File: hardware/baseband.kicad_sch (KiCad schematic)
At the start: 36 parts, among them U503 MCP4551, U504 MCP4551, U6 MCP6002, U7 MCP6002

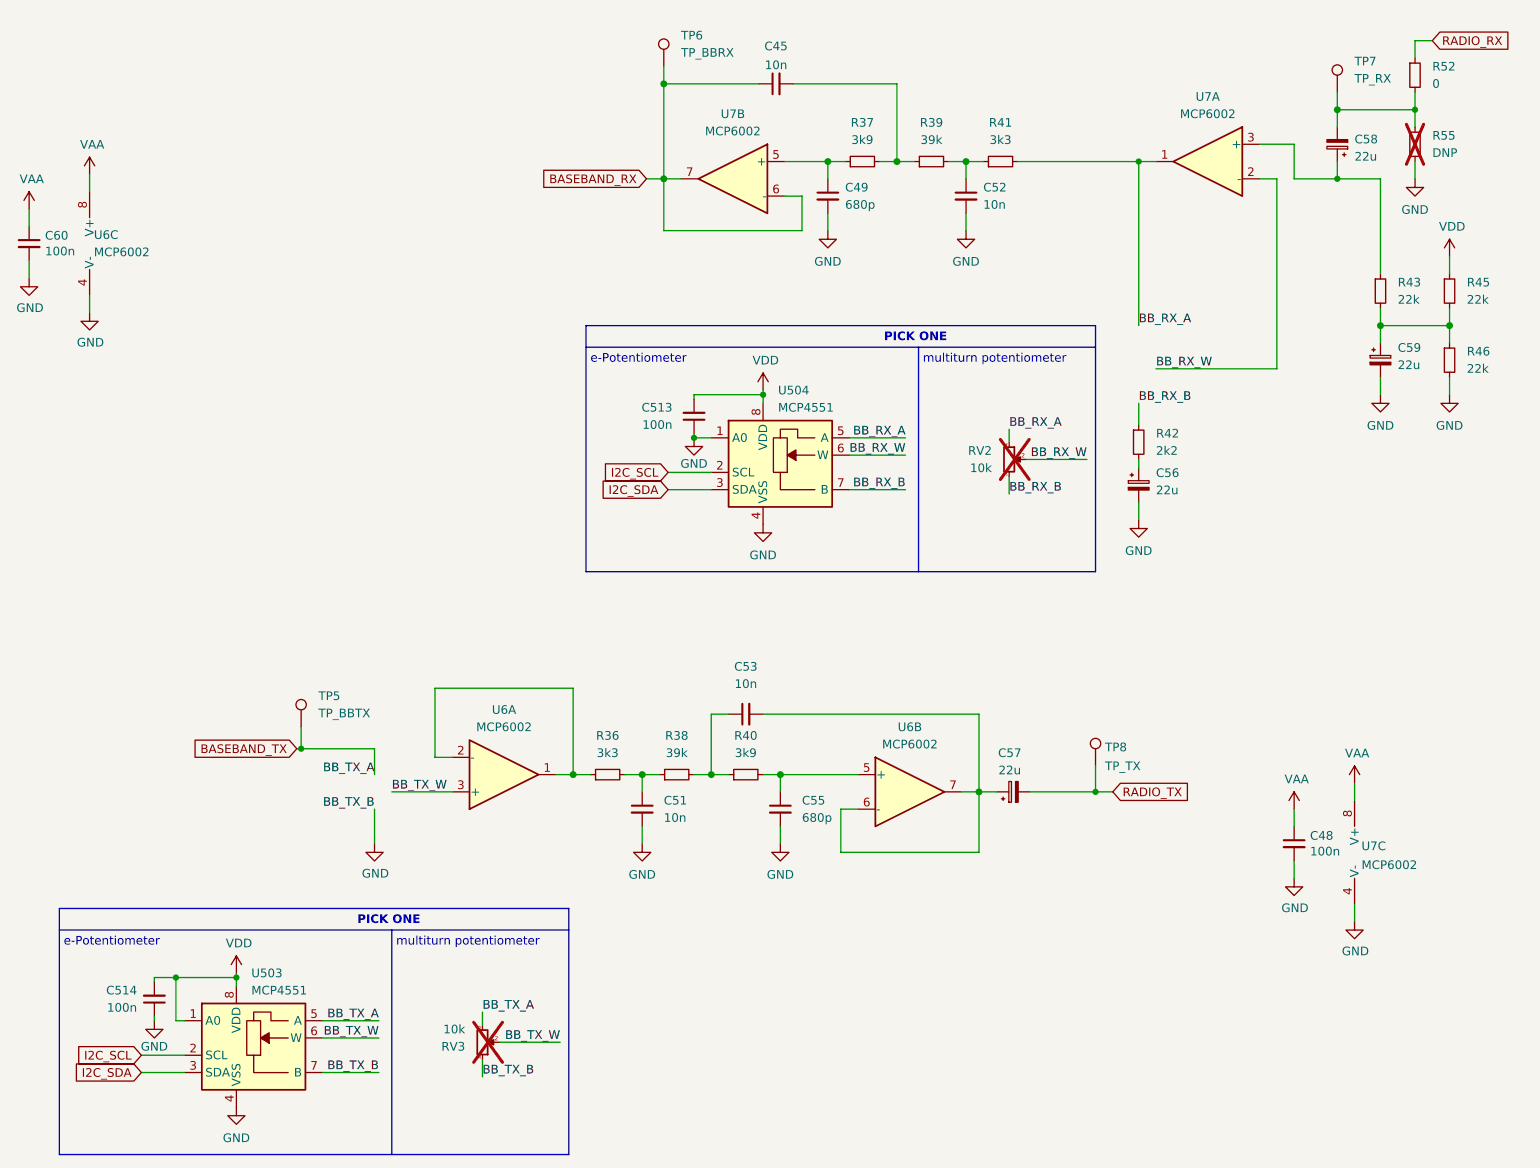
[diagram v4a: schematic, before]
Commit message: Switched to M17_kicad_library for custom symbols/footprints
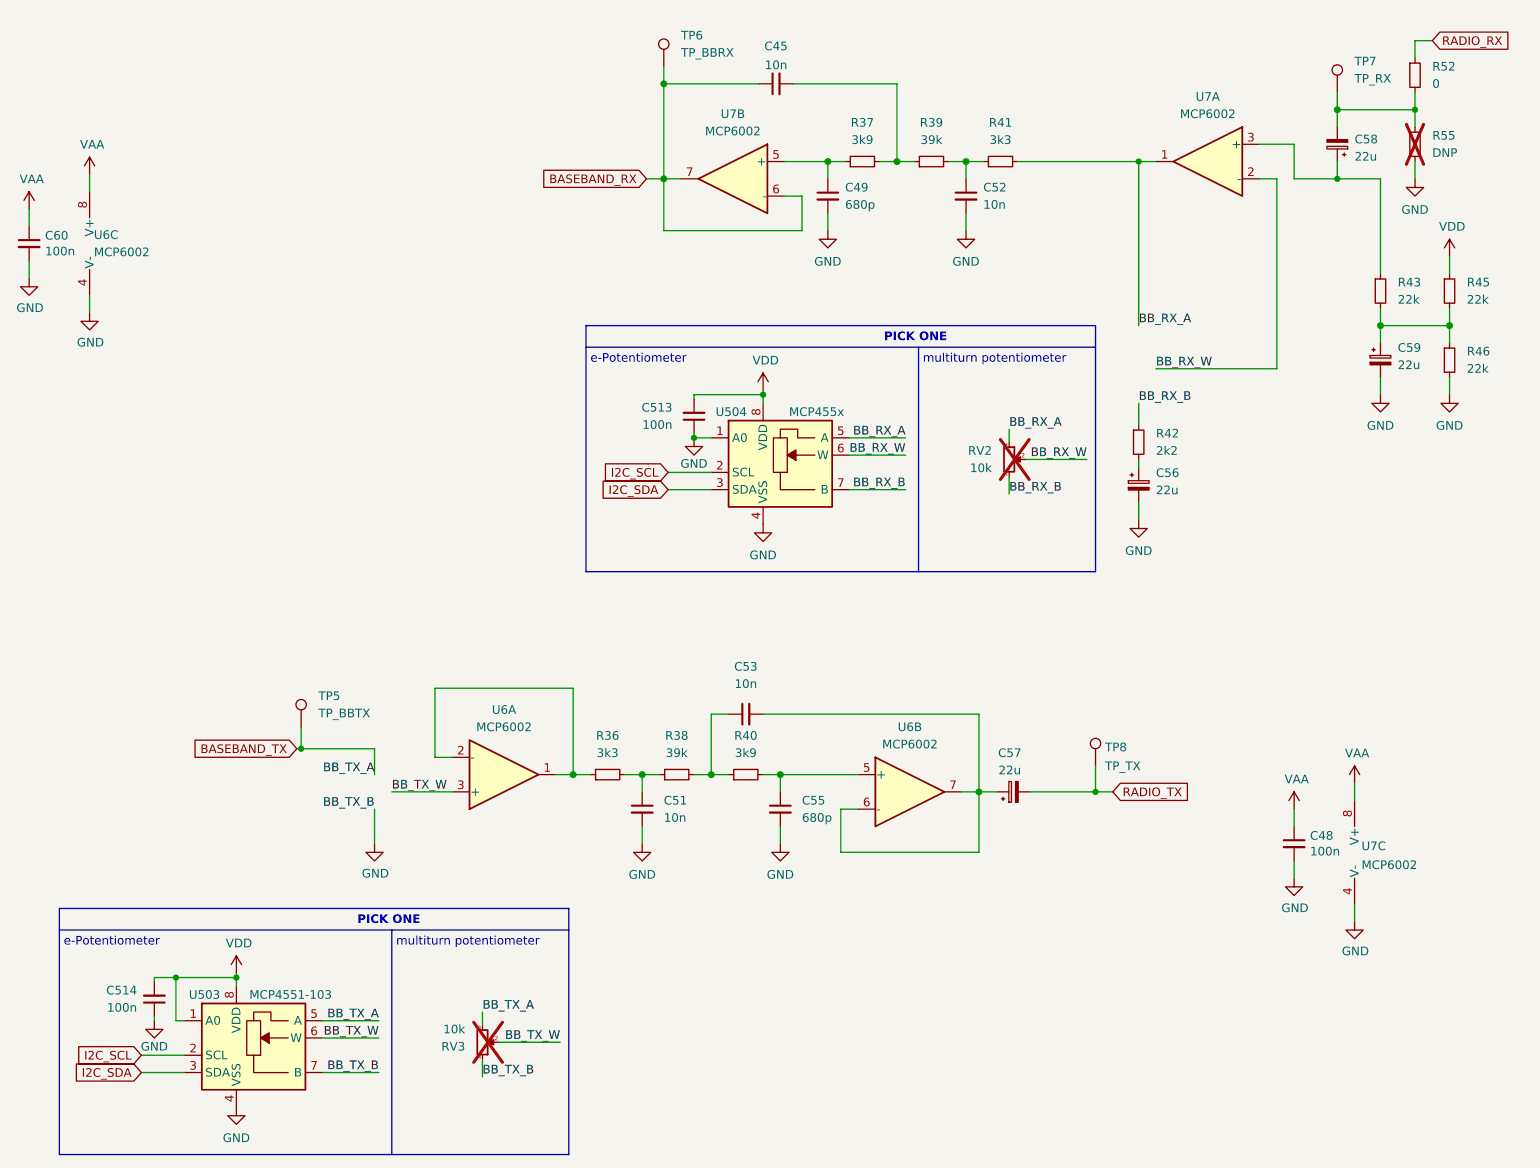
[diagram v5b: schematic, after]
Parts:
- removed U503, U504: MCP4551, Package_SO:MSOP-8_3x3mm_P0.65mm, symbol Module17:MCP4551
- added U503: MCP4551-103, Package_SO:MSOP-8_3x3mm_P0.65mm, symbol M17_misc_active:MCP455x
- added U504: MCP455x, Package_SO:MSOP-8_3x3mm_P0.65mm, symbol M17_misc_active:MCP455x
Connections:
- net BASEBAND_TX: now also U503.5 (A)
- net BB_RX_A: now also U504.5 (A)
- net BB_RX_B: now also U504.7 (B)
- net BB_RX_W: now also U504.6 (W)
- net BB_TX_W: now also U503.6 (W)
- net GND: now also U503.4 (VSS), U503.7 (B), U504.1 (A0), U504.4 (VSS)
- net I2C_SCL: now also U503.2 (SCL), U504.2 (SCL)
- net I2C_SDA: now also U503.3 (SDA), U504.3 (SDA)
- net VDD: now also U503.1 (A0), U503.8 (VDD), U504.8 (VDD)

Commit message: Updated various MPNs
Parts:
- C513, C514: MPN (none) -> Generic C/100nF/C0G/25V/0603
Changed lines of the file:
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@@
+      (effects (font (size 1.27 1.27)) hide)
+    )
+    (property "MPN" "Generic C/100nF/C0G/25V/0603" (at 50.8 164.465 0)
       (effects (font (size 1.27 1.27)) hide)
     )
@@
       (effects (font (size 1.27 1.27)) hide)
     )
+    (property "MPN" "Generic C/100nF/C0G/25V/0603" (at 130.175 78.74 0)
+      (effects (font (size 1.27 1.27)) hide)
+    )

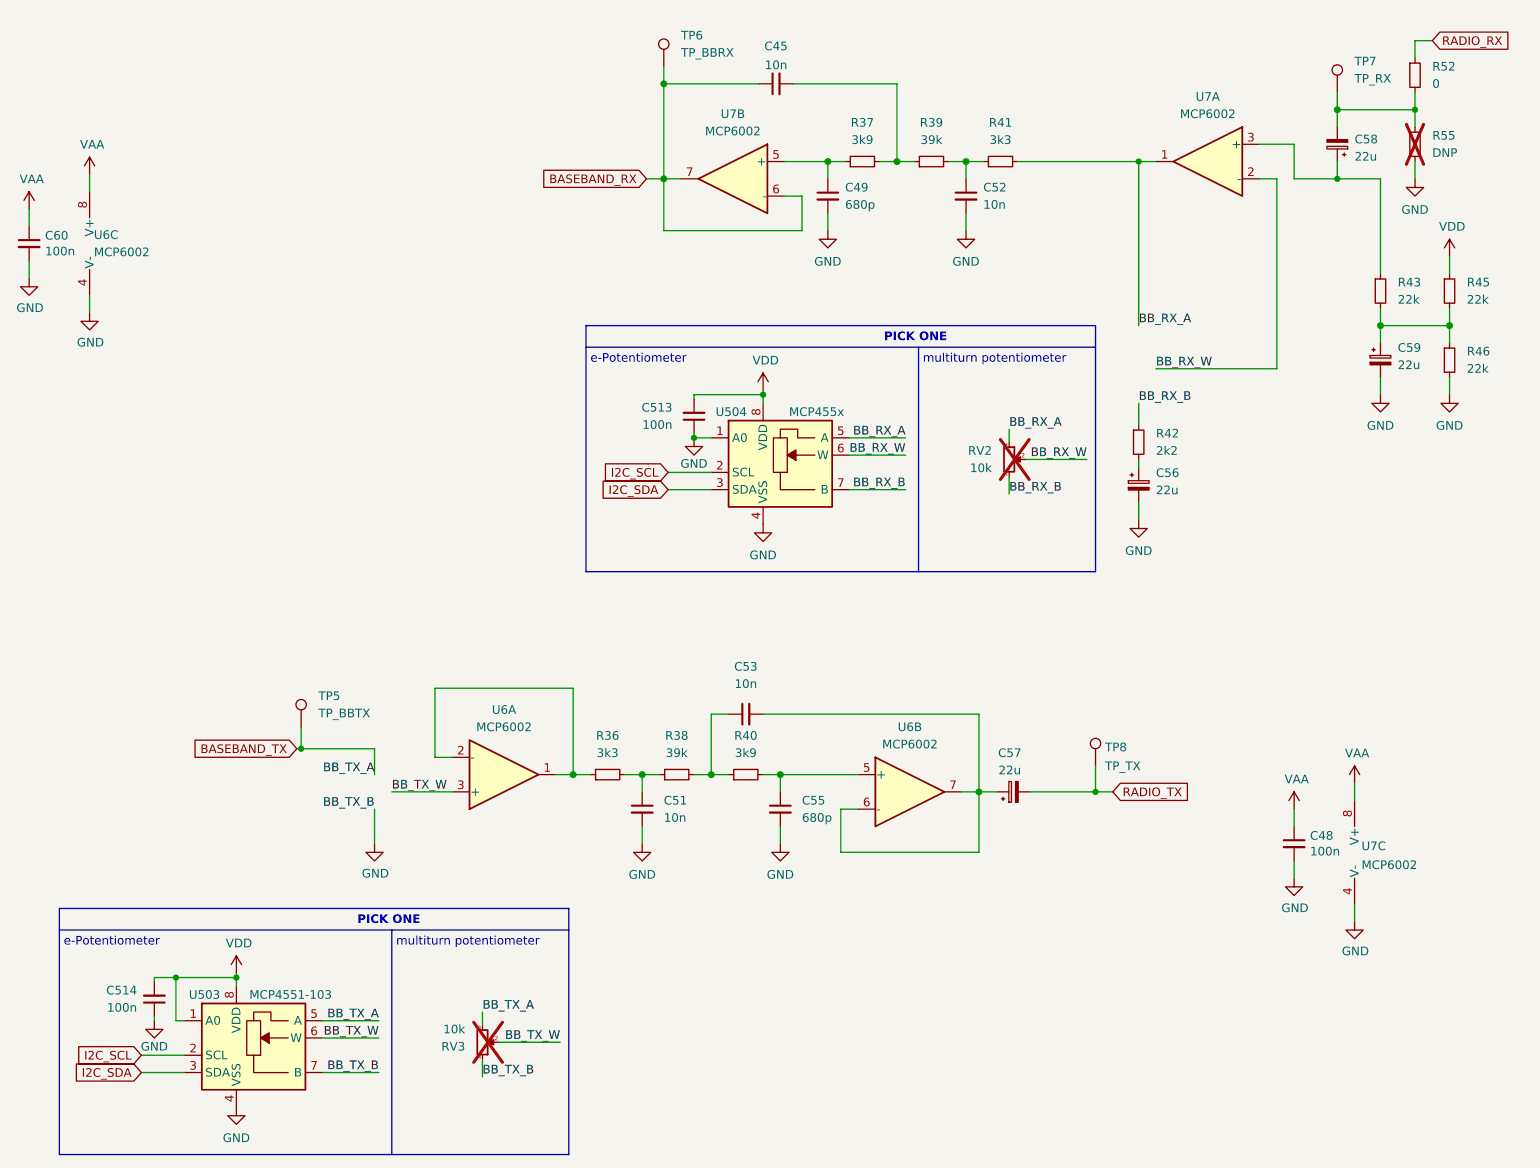
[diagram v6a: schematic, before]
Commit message: Reworked schematic
Rearranged disposition and renumbered components
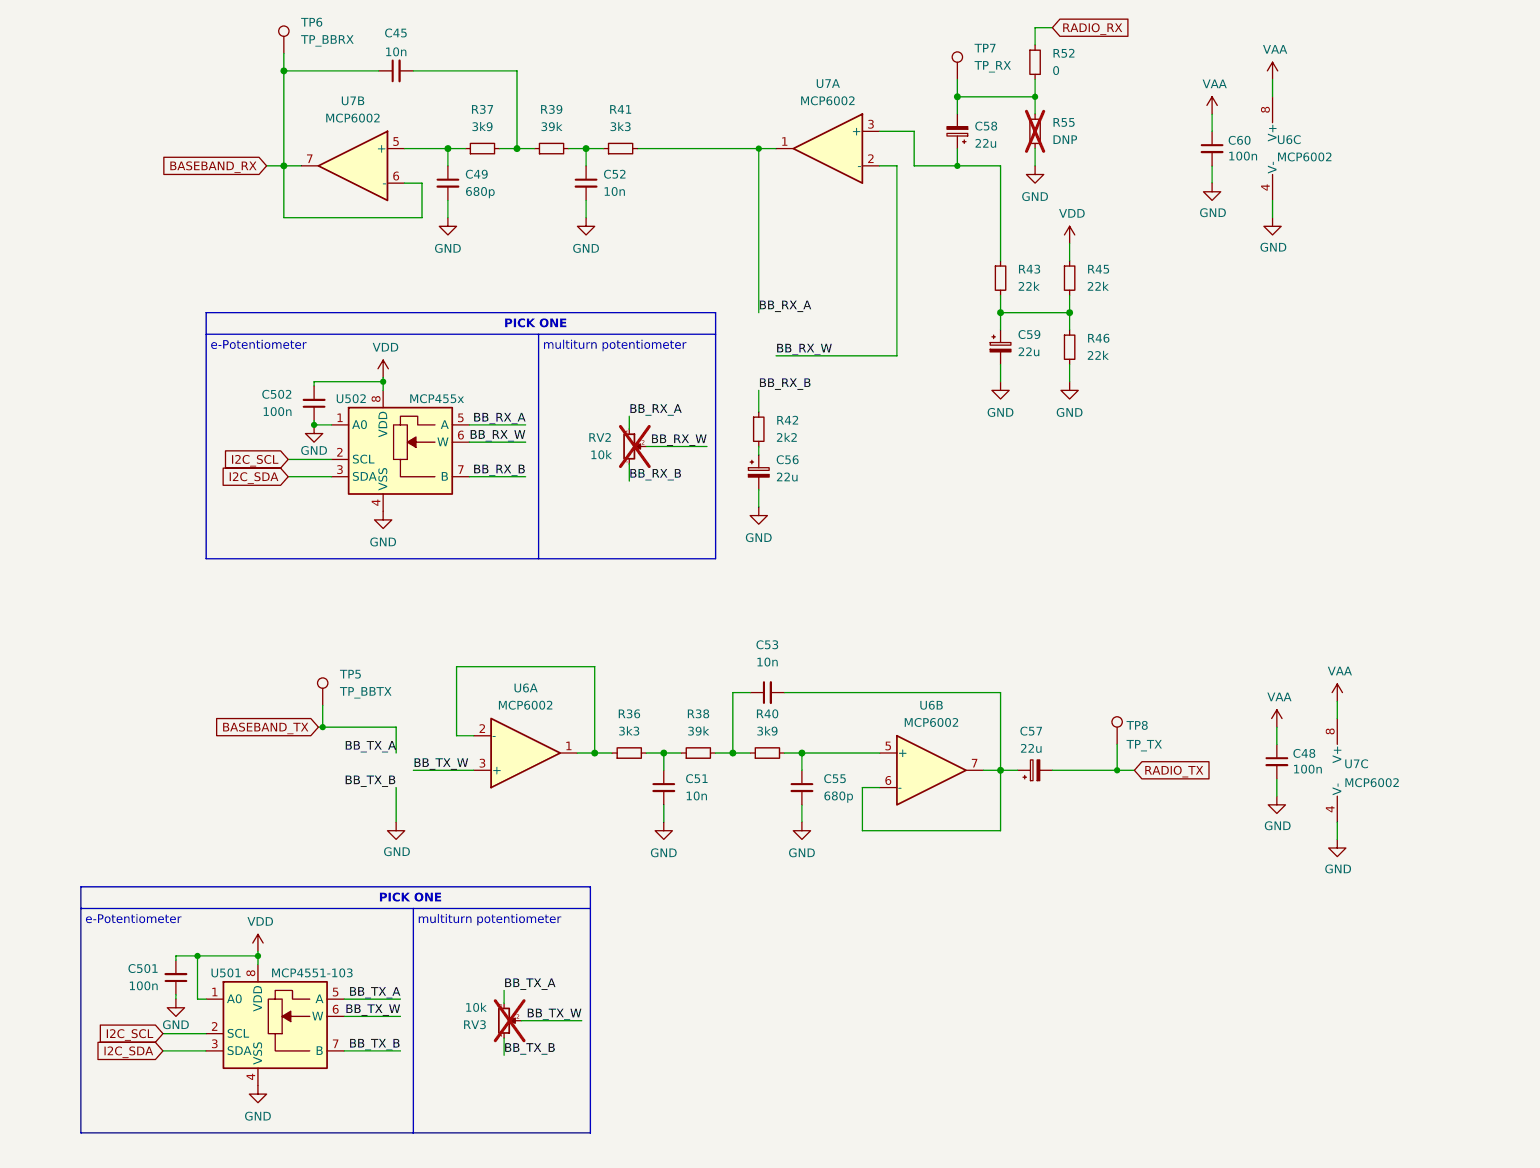
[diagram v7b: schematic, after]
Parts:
- renumbered C514 to C501, C513 to C502, U503 to U501, U504 to U502
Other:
- moved on the sheet: C45, C48, C49, C501, C502, C51, C52, C53, C55, C56, C57, C58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
